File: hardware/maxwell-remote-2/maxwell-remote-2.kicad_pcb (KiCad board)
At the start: 2 copper layers, 71 x 38 mm, 21 parts, among them J1 INPUT, J2 Left, J3 Right, J4 DISPLAY, J5 FPC-1, J6 FPC-2, J7 SPI1_A, J8 SPI1_B, J9 SPI1_C, Q1 NDS332P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

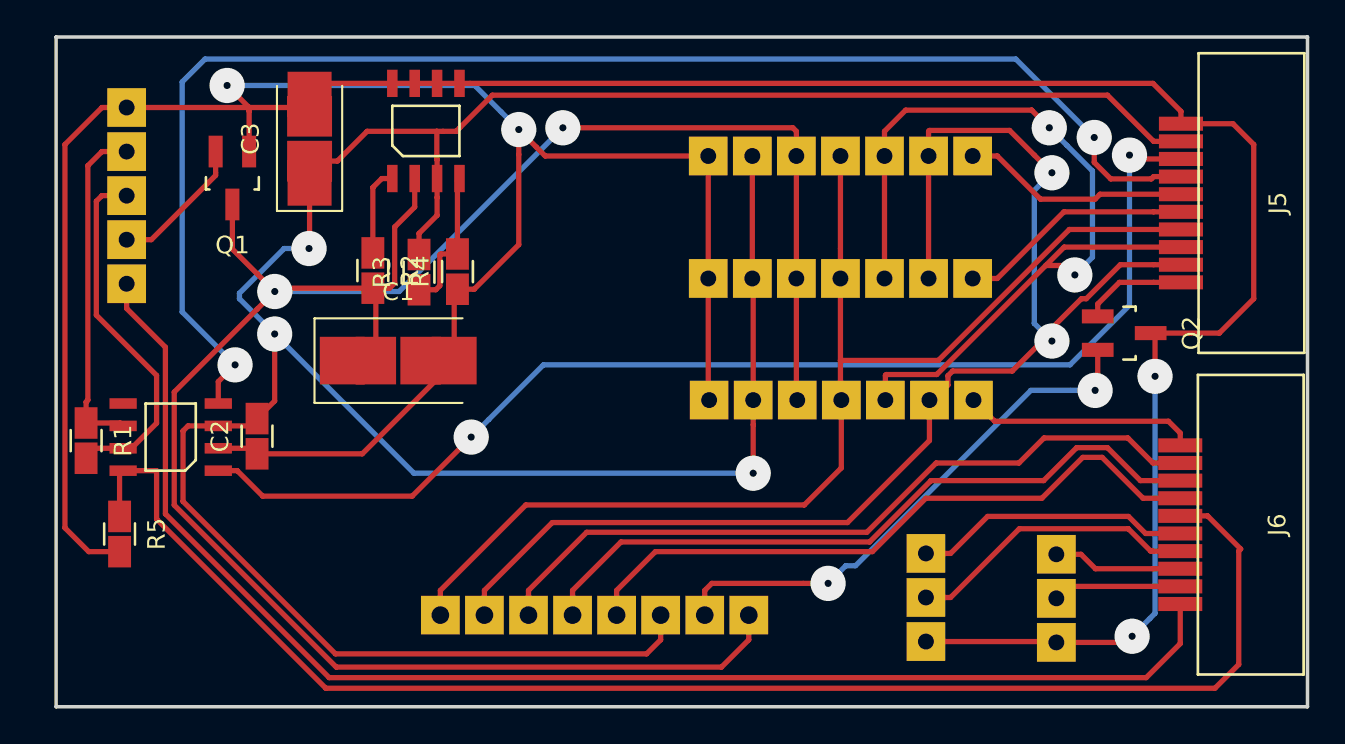
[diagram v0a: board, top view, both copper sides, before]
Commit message: Finishing-up secondary connector board.
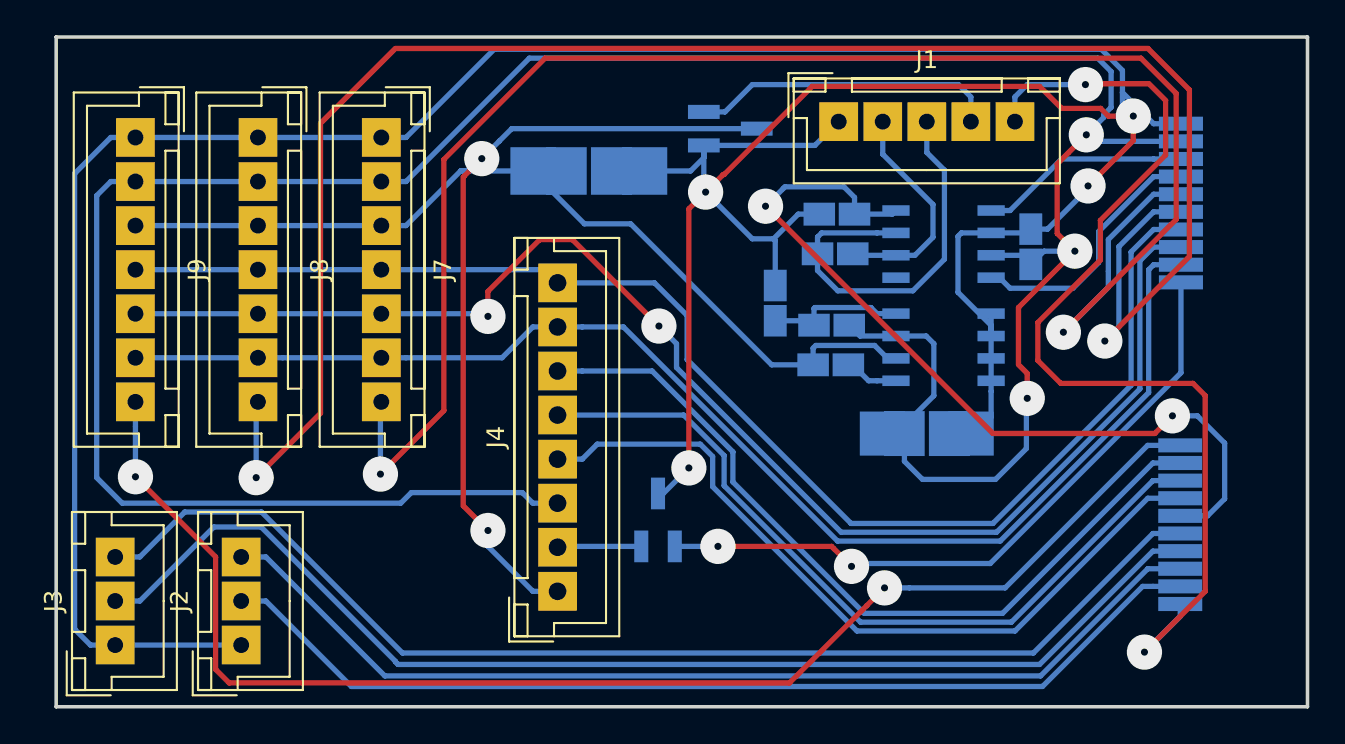
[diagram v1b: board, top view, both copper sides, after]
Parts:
- C1, C2, C3, J5, J6, Q1, Q2, R1, R2, R3, R4, R5, U1, U2: moved to B.Cu
- J1, J2, J3, J4, J7, J8, J9: moved to F.Cu
- moved J2 46.3 mm to (157.5, 83.5)
- moved J3 46.0 mm to (150.3, 83.5)
- moved C2 45.2 mm to (202.3, 60.9), turned to 270 degrees
- moved U1 45.2 mm to (197.3, 60.8)
- moved R5 44.6 mm to (191.3, 59.0), turned to 180 degrees
- moved R1 43.8 mm to (191.2, 61.3), turned to 180 degrees
- moved J1 40.4 mm to (191.4, 53.8), turned to 0 degrees
- moved C3 38.8 mm to (196.4, 71.5), turned to 0 degrees
- moved J9 35.8 mm to (151.5, 54.7), turned to 270 degrees
- moved U2 31.8 mm to (197.3, 66.6), turned to 0 degrees
- moved Q2 28.5 mm to (181.2, 76.4), turned to 180 degrees
- moved Q1 28.4 mm to (185.2, 54.2), turned to 90 degrees
- moved J8 26.8 mm to (158.4, 54.7), turned to 270 degrees
- moved R2 26.5 mm to (190.9, 67.6), turned to 180 degrees
- moved R3 23.6 mm to (191.0, 65.3), turned to 0 degrees
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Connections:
- J5 pad 1: GND -> ENABLE_SCREEN
- J5 pad 10: ENABLE_SCREEN -> GND
- J5 pad 2: +3V3 -> SPI1_SCK
- J5 pad 3: CAN_TX -> SPI1_MISO
- J5 pad 4: CAN_RX -> SPI1_MOSI
- J5 pad 5: ~SPI1_CS_2 -> ~SPI1_CS_3
- J5 pad 6: ~SPI1_CS_3 -> ~SPI1_CS_2
- J5 pad 7: SPI1_MOSI -> CAN_RX
- J5 pad 8: SPI1_MISO -> CAN_TX
- J5 pad 9: SPI1_SCK -> +3V3
- J6 pad 1: ~SPI_CS_4 -> WAKE
- J6 pad 10: WAKE -> ~SPI_CS_4
- J6 pad 2: SCREEN_A0 -> ~LEFT_A
- J6 pad 3: ~SCREEN_RST -> ~LEFT_B
- J6 pad 4: ~SCREEN_CS -> ~RIGHT_A
- J6 pad 5: ~ENABLE_CAN -> ~RIGHT_B
- J6 pad 6: ~RIGHT_B -> ~ENABLE_CAN
- J6 pad 7: ~RIGHT_A -> ~SCREEN_CS
- J6 pad 8: ~LEFT_B -> ~SCREEN_RST
- J6 pad 9: ~LEFT_A -> SCREEN_A0
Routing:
- net ~SPI1_CS_3: track 13.4 -> 104.3 mm, vias 0 -> 2
- net ~SPI1_CS_2: track 13.0 -> 95.9 mm, vias 0 -> 2
- net CAN_RX: track 80.8 -> 14.7 mm, vias 2 -> 0
- net ~SPI_CS_4: track 13.2 -> 77.7 mm, vias 0 -> 2
- net CAN_TX: track 68.3 -> 12.0 mm, vias 2 -> 0
- net ~RIGHT_B: track 15.7 -> 67.6 mm
- net ~RIGHT_A: track 16.6 -> 68.1 mm
- net ~LEFT_B: track 7.37 -> 58.6 mm
- net ~LEFT_A: track 7.31 -> 57.6 mm
- net ~ENABLE_CAN: track 84.1 -> 47.7 mm, vias 0 -> 2
- net ENABLE_SCREEN: track 5.93 -> 38.9 mm, vias 0 -> 2
- net SPI1_MISO: track 51.4 -> 80.6 mm
- net +BATT: track 127.1 -> 98.1 mm
- net Net-(J4-Pad2): track 30.6 -> 4.77 mm, vias 2 -> 0
- net WAKE: track 78.4 -> 58.3 mm, vias 0 -> 2
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
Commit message: Updating for manufacture.
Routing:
- added copper zone on B.Cu, net GND
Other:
- board text added: "- A B"
- board text added: "CAN"
- board text added: "DISP"
- board text added: "L"
- board text added: "R"
- board text added: "S-A"
- board text added: "S-B"
- board text added: "S-C"
- board text added: "maxwell-remote-2 v5.0 @coddingtonbear 24 June 2018"
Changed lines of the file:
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@@
   (general
     (thickness 1.6)
-    (drawings 4)
+    (drawings 13)
     (tracks 382)
     (zones 0)
@@
       (outputformat 1)
       (mirror false)
-      (drillshape 1)
+      (drillshape 0)
       (scaleselection 1)
       (outputdirectory ""))
@@
       (rotate (xyz 0 0 0))
     )
+  )
+  (gr_text "maxwell-remote-2 v5.0\n@coddingtonbear\n24 June 2018" (at 198 75) (layer F.SilkS)
+    (effects (font (size 1 1) (thickness 0.25)))
+  )
+  (gr_text DISP (at 181 81 90) (layer F.SilkS)
+    (effects (font (size 1.5 1.5) (thickness 0.3)))
+  )
+  (gr_text CAN (at 191 59) (layer F.SilkS)
+    (effects (font (size 1.5 1.5) (thickness 0.3)))
+  )
+  (gr_text S-C (at 150 51) (layer F.SilkS)
+    (effects (font (size 1.5 1.5) (thickness 0.3)))
+  )
+  (gr_text S-B (at 157 51) (layer F.SilkS)
+    (effects (font (size 1.5 1.5) (thickness 0.3)))
+  )
+  (gr_text S-A (at 164 51) (layer F.SilkS)
+    (effects (font (size 1.5 1.5) (thickness 0.3)))
+  )
+  (gr_text L (at 155 74) (layer F.SilkS)
+    (effects (font (size 1.5 1.5) (thickness 0.3)))
+  )
+  (gr_text R (at 148 74) (layer F.SilkS)
+    (effects (font (size 1.5 1.5) (thickness 0.3)))
+  )
+  (gr_text "- A B" (at 163 81 90) (layer F.SilkS)
+    (effects (font (size 1.5 1.5) (thickness 0.3)))
   )
   (gr_line (start 218 87) (end 218 49) (layer Edge.Cuts) (width 0.2))
@@
   (segment (start 195.725 61.385) (end 196.75 60.36) (width 0.3) (layer B.Cu) (net 28))
   (segment (start 196.75 60.36) (end 196.75 58.5) (width 0.3) (layer B.Cu) (net 28))
+  (zone (net 1) (net_name GND) (layer B.Cu) (hatch edge 0.508)
+    (connect_pads (clearance 0.508))
+    (min_thickness 0.254)
+    (fill yes (arc_segments 16) (thermal_gap 0.508) (thermal_bridge_width 0.508))
+    (polygon
+      (pts
+        (xy 218 49) (xy 147 49) (xy 147 87) (xy 218 87)
+      )
+    )
+  )
 )

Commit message: Fixing footprint for MOSFET packages; enable/disable VBATT instead of GND for screen.
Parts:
- Q1: footprint cuzdaori/KiCad.pretty:SOT-23_Handsoldering -> re-innovation/kicad_reinnovation/KiCAD PRETTY/TO_SOT_Packages_SMD.pretty:SOT-23_Handsoldering
- Q2: value BSS138P -> NDS332P; footprint cuzdaori/KiCad.pretty:SOT-23_Handsoldering -> re-innovation/kicad_reinnovation/KiCAD PRETTY/TO_SOT_Packages_SMD.pretty:SOT-23_Handsoldering
- moved Q2 12.4 mm to (169.0, 79.0)
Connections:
- J4 pad 1: +BATT -> Net-(J4-Pad1)
- J4 pad 2: Net-(J4-Pad2) -> GND
- Q2 pad 2: GND -> Net-(J4-Pad1)
- Q2 pad 3: Net-(J4-Pad2) -> +BATT
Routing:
- net Net-(J4-Pad1): track 0.00 -> 18.1 mm
- net ENABLE_SCREEN: track 38.9 -> 52.4 mm
- net +BATT: track 98.1 -> 90.6 mm
- net Net-(J4-Pad2): track 4.77 -> 0.00 mm
- net Net-(J1-Pad4): track 17.5 -> 14.6 mm
- net GND: track 209.9 -> 211.9 mm
